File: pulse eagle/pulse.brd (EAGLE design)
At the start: 39.2 x 20.7 mm, 18 parts, among them J1 ISP Touch, U1 ATMEGA328P, Y1 16MHz

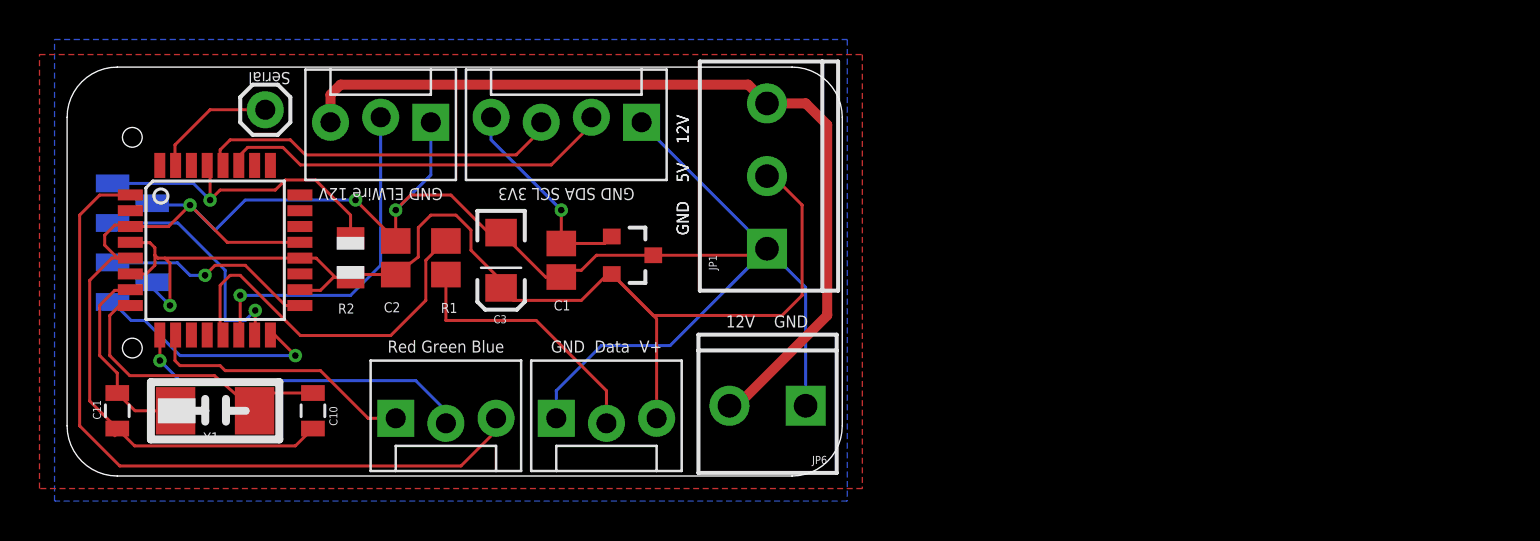
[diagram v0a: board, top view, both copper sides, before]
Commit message: Adding extra stem led and three extra petal leds. Needs routing.
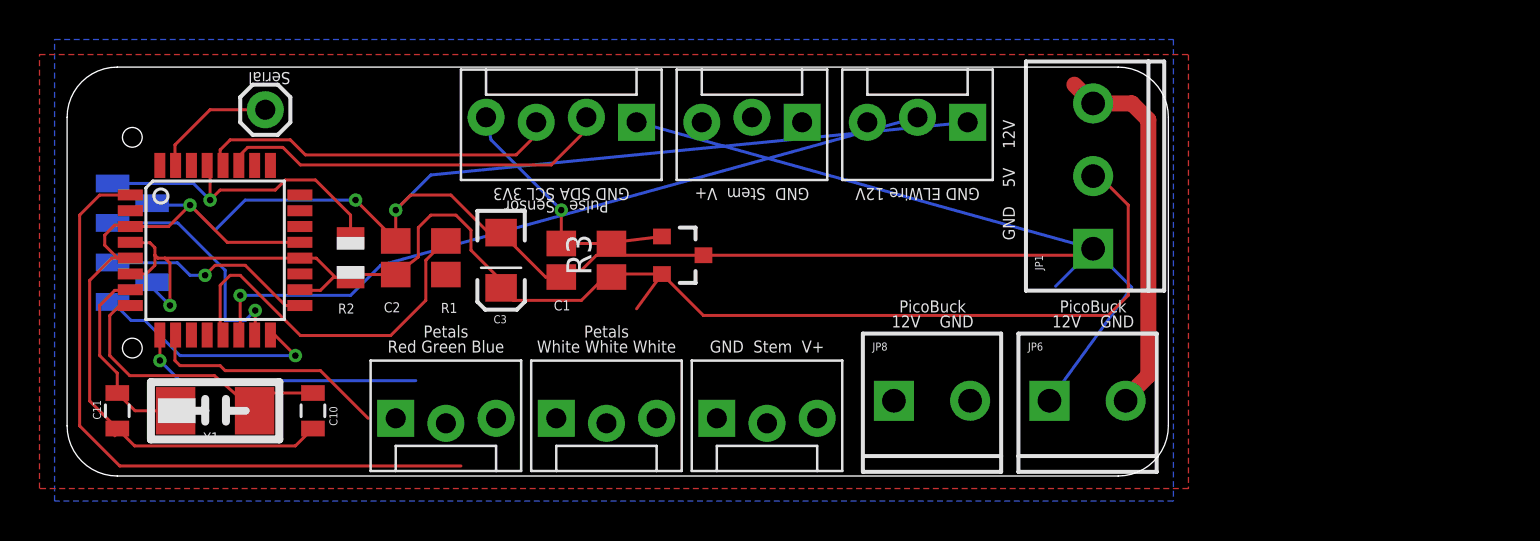
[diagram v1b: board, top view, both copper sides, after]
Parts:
- added JP7, JP9: (no value), SparkFun-Connectors:MOLEX-1X3_LOCK
- added JP8: M023.5MM_LOCK, SparkFun-Connectors:SCREWTERMINAL-3.5MM-2_LOCK
- added R3: 220, resistor:R0805
- moved JP3 27.2 mm to (46.2, 18.8)
- moved JP1 16.5 mm to (52.6, 12.4)
- moved JP6 12.7 mm to (50.5, 4.57), turned to 0 degrees
- moved JP4 8.13 mm to (33.5, 3.56)
- moved U$1 2.54 mm to (31.8, 11.9)
- moved SL2 0.25 mm to (29.5, 18.8)
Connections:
- new net N$1: JP9.2, R3.2
- new net PETALWHITE: JP7.1, JP7.2, JP7.3, U1.13
- new net STEMLED2: R3.1, U1.11
- net 12V: now also JP8.2
- net GND: now also JP8.1, JP9.1
- net STEMLED: now also U1.12; no longer U1.13
- net VCC: now also JP9.3
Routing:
- net GND: track 112.5 -> 154.7 mm
- net 12V: track 44.1 -> 19.4 mm
- net ELWIRE: track 17.3 -> 38.0 mm
- net N$7: track 13.6 -> 0.00 mm
- net VCC: track 64.8 -> 75.2 mm
- net PETALBLUE: track 37.0 -> 33.8 mm
- net PETALGREEN: track 17.5 -> 14.7 mm
- net 3V3: track 10.6 -> 13.0 mm
- net PETALRED: track 13.7 -> 12.3 mm
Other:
- board size 39.2 x 20.7 mm -> 55.8 x 20.7 mm
- board text added: "GND Stem V+"
- board text added: "Petals"
- board text added: "PicoBuck"
- board text added: "Pulse Sensor"
- board text added: "White White White"
- board text removed: "GND Data V+"

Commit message: Revision 5 of the board, with 4 x Petals, 2 x Stem.
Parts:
- JP1: value (none) -> Power
- JP4, JP9: value (none) -> Stem
- JP6: value M023.5MM_LOCK -> Petal Center
- JP8: value M023.5MM_LOCK -> Petal Color
- SL2: value (none) -> Pulse Sensor
- moved JP7 19.7 mm to (25.4, 3.56), turned to 0 degrees
- moved JP9 19.7 mm to (37.8, 18.8), turned to 180 degrees
- moved C10 0.51 mm to (13.1, 3.56)
- moved C11 0.51 mm to (3.17, 3.56)
- moved Y1 0.51 mm to (8.13, 3.56)
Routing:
- net PETALWHITE: track 0.00 -> 27.0 mm, vias 0 -> 1
- net VCC: track 75.2 -> 102.2 mm, vias 1 -> 2
- net STEMLED2: track 0.00 -> 24.5 mm
- net 12V: track 19.4 -> 40.9 mm
- net N$7: track 0.00 -> 21.0 mm, vias 0 -> 1
- net GND: track 154.7 -> 169.6 mm
- net N$1: track 0.00 -> 12.1 mm
- net ELWIRE: track 38.0 -> 43.0 mm
- net PETALBLUE: track 33.8 -> 37.2 mm
- net PETALGREEN: track 14.7 -> 17.5 mm
- net PETALRED: track 12.3 -> 13.7 mm
- net MISO: track 12.1 -> 12.8 mm
- net 3V3: track 13.0 -> 13.6 mm
- net XTL1: track 10.0 -> 10.5 mm
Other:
- board text added: "GND Data 5V"
- board text added: "Pulse & Bloom 23 June 2014 - Rev. 5"
- board text added: "Stem"
- board text removed: "GND Stem V+"
- board text removed: "Pulse & Bloom 19 June 2014 - Rev. 4"
- board text removed: "Pulse Sensor"

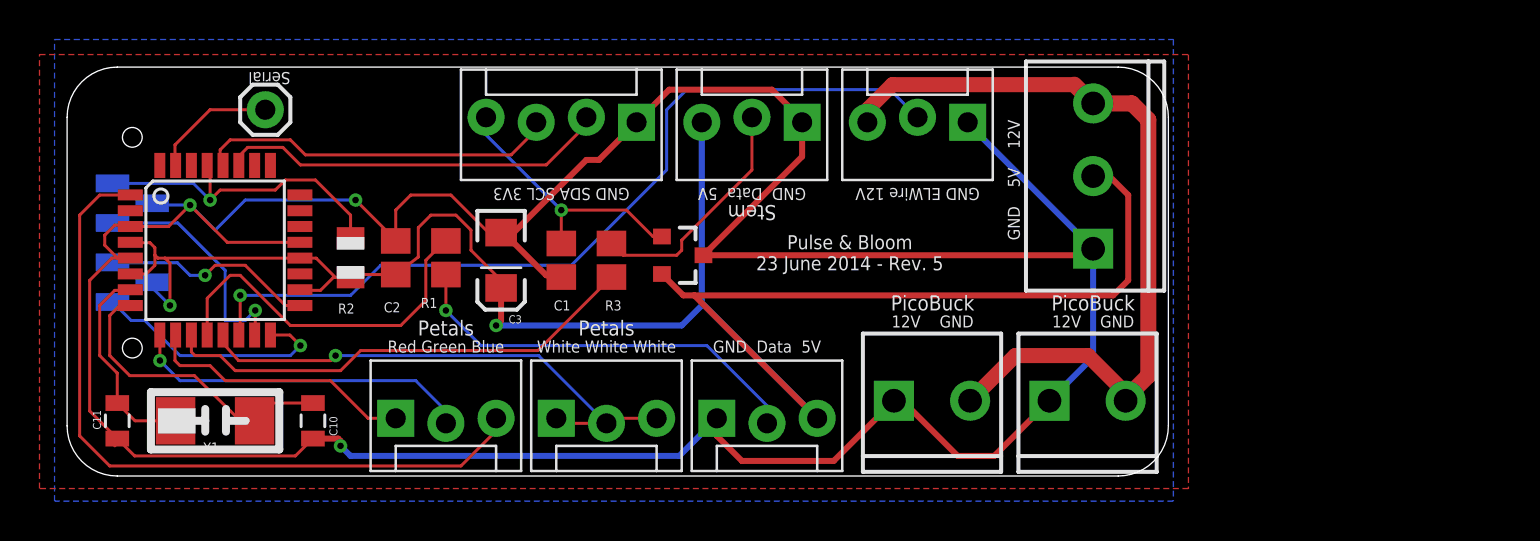
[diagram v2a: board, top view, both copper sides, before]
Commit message: Adding extra gnd pins for picobucks. probably going to need more picobucks.
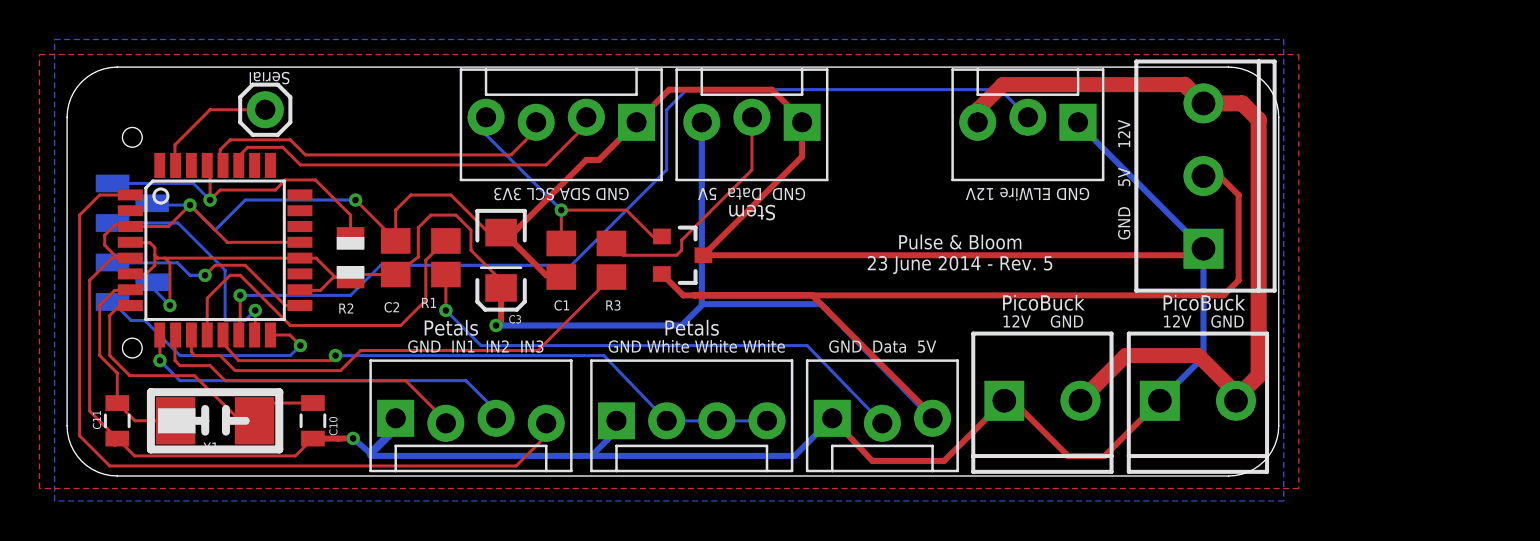
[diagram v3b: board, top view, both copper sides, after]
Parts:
- JP5: device SparkFun-Connectors:MOLEX-1X3_LOCK -> SparkFun-Connectors:MOLEX-1X4_LOCK
- JP7: device SparkFun-Connectors:MOLEX-1X3_LOCK -> SparkFun-Connectors:MOLEX-1X4
- moved JP4 5.84 mm to (39.4, 3.56)
- moved JP3 5.59 mm to (51.8, 18.8)
- moved JP6 5.59 mm to (56.1, 4.57)
- moved JP8 5.59 mm to (48.3, 4.57)
- moved JP1 5.59 mm to (58.2, 12.4)
- moved JP7 3.05 mm to (28.4, 3.56)
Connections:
- net GND: now also JP5.1, JP7.1
- net PETALBLUE: now also JP5.4; no longer JP5.3
- net PETALGREEN: now also JP5.3; no longer JP5.2
- net PETALRED: now also JP5.2; no longer JP5.1
- net PETALWHITE: now also JP7.4; no longer JP7.1
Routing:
- net VCC: track 102.2 -> 119.6 mm
- net GND: track 169.6 -> 184.8 mm
- net ELWIRE: track 43.0 -> 48.6 mm
- net N$7: track 21.0 -> 26.3 mm
- net PETALWHITE: track 27.0 -> 29.9 mm
- net PETALRED: track 13.7 -> 16.4 mm
- net PETALBLUE: track 37.2 -> 39.7 mm
- net PETALGREEN: track 17.5 -> 19.7 mm
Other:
- board size 55.8 x 20.7 mm -> 61.3 x 20.7 mm
- board text added: "GND IN1 IN2 IN3"
- board text added: "GND White White White"
- board text removed: "Red Green Blue"
- board text removed: "White White White"

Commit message: Adding second pulse sensor to board and code. Need to write code to handle second pulse sensor and second stem.
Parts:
- added SL1: Pulse Sensor, SparkFun-Connectors:MOLEX-1X4_LOCK
- moved JP9 5.59 mm to (43.4, 18.8)
- moved SL2 5.33 mm to (34.8, 18.8)
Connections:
- new net SCL2: SL1.3, U1.24
- new net SDA2: SL1.2, U1.23
- net 3V3: now also SL1.4
- net GND: now also SL1.1
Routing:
- net GND: track 184.8 -> 203.2 mm
- net SDA2: track 0.00 -> 17.0 mm, vias 0 -> 1
- net SCL2: track 0.00 -> 16.2 mm, vias 0 -> 1
- net 3V3: track 13.6 -> 25.1 mm
- net N$1: track 12.1 -> 17.6 mm
- net SDA: track 19.8 -> 25.2 mm
- net SCL: track 18.3 -> 23.6 mm
- net VCC: track 119.6 -> 114.5 mm
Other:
- board text added: "Pulse & Bloom 24 June 2014 - Rev. 6"
- board text removed: "Pulse & Bloom 23 June 2014 - Rev. 5"

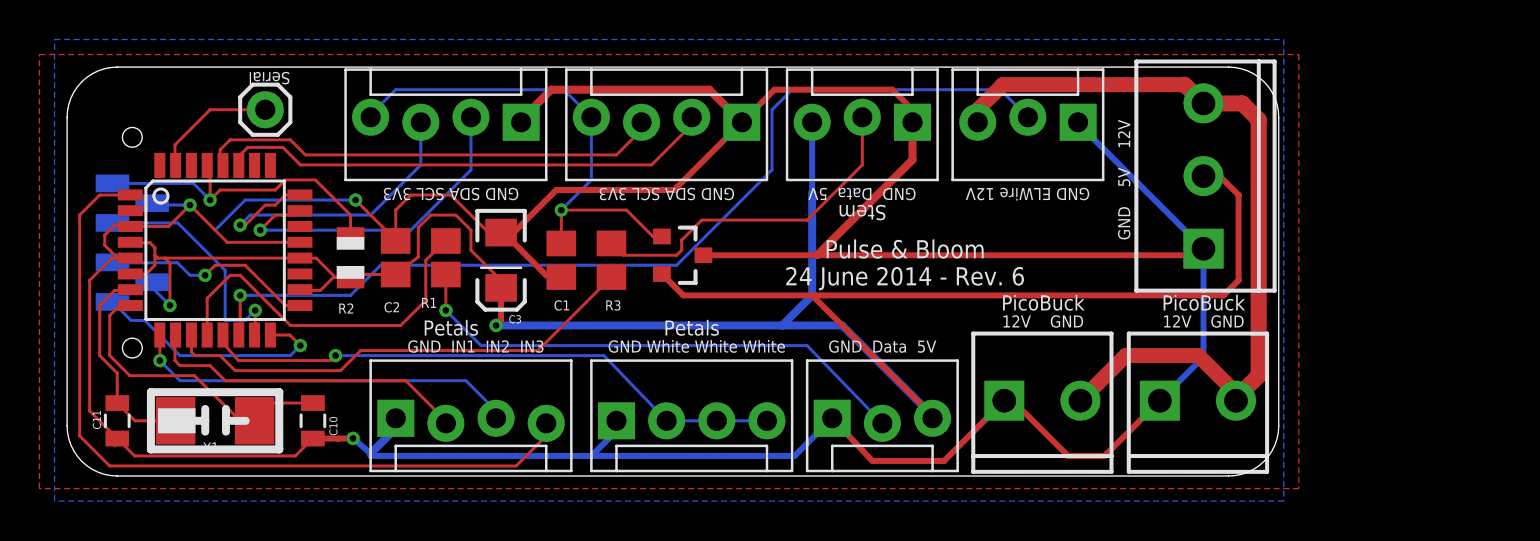
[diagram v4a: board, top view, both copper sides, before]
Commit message: Adding a barrel jack and proper buck converter connectors.
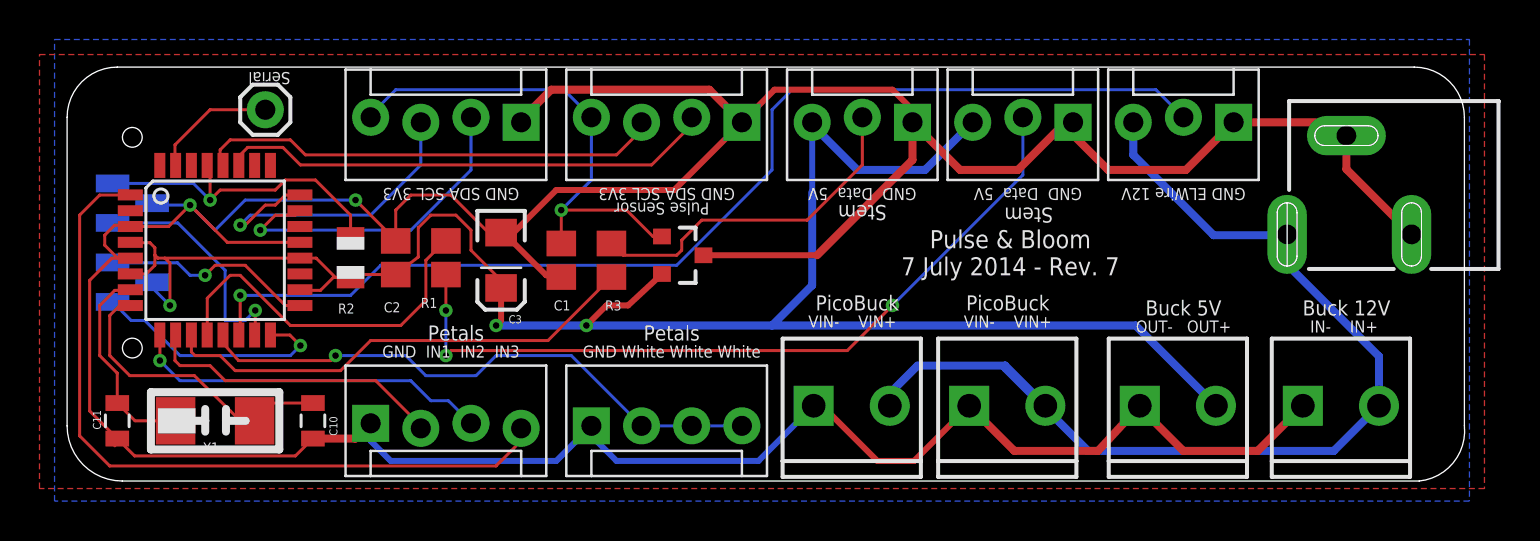
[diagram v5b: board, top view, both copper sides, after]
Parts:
- removed JP1: Power, SparkFun-Connectors:SCREWTERMINAL-3.5MM-3_LOCK.007S
- added J2: POWER_JACKSLT, SparkFun-Connectors:POWER_JACK_SLOT
- added JP10: Buck 12V, SparkFun-Connectors:SCREWTERMINAL-3.5MM-2_LOCK
- added JP12: Buck 5V, SparkFun-Connectors:SCREWTERMINAL-3.5MM-2_LOCK
- moved JP4 19.5 mm to (51.6, 18.8), turned to 180 degrees
- moved JP6 9.66 mm to (46.5, 4.32)
- moved JP8 9.66 mm to (38.6, 4.32)
- moved JP3 7.87 mm to (59.7, 18.8)
- moved JP5 1.30 mm to (16.0, 3.30)
- moved JP7 1.30 mm to (27.2, 3.30)
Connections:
- net 12V: now also J2.PWR, JP10.2; no longer JP1.3
- net GND: now also J2.GND@1, J2.GND@2, JP10.1, JP12.1; no longer JP1.1
- net VCC: now also JP12.2; no longer JP1.2
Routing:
- net VCC: track 114.5 -> 98.6 mm, vias 2 -> 3
- net N$7: track 26.3 -> 40.0 mm, vias 1 -> 3
- net 12V: track 40.9 -> 53.4 mm
- net ELWIRE: track 48.6 -> 56.5 mm
- net GND: track 203.2 -> 206.8 mm, vias 3 -> 2
- net PETALGREEN: track 19.7 -> 18.4 mm
- net PETALBLUE: track 39.7 -> 38.3 mm
- net PETALRED: track 16.4 -> 15.2 mm
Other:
- board size 61.3 x 20.7 mm -> 70.8 x 21 mm
- board text added: "IN- IN+"
- board text added: "OUT- OUT+"
- board text added: "Pulse & Bloom 7 July 2014 - Rev. 7"
- board text added: "VIN- VIN+"
- board text removed: "12V GND"
- board text removed: "GND 5V 12V"
- board text removed: "Pulse & Bloom 24 June 2014 - Rev. 6"
